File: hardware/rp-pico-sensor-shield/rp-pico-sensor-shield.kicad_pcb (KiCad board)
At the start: 2 copper layers, 87 x 65 mm, 39 parts, among them J1 Barrel_Jack, J10 Conn_01x04, J11 Conn_01x04, J12 Conn_01x04, J13 Conn_01x04, J14 Conn_01x04, J15 Conn_01x04, J16 Conn_01x04, J17 Conn_01x03, J18 Conn_01x03, J19 Conn_01x03, J2 Conn_01x04, J20 Conn_01x03, J21 Conn_01x03, J22 Conn_01x03, J23 Conn_01x04, J24 Screw Terminal, J25 Conn_01x04, J26 I2C0, J27 I2C1, J28 AGND, J29 Conn_01x03, J3 Conn_01x04, J4 Conn_01x04, J5 Conn_01x04, J6 Conn_01x04, J7 Conn_01x04, J8 Conn_01x04, J9 Conn_01x04, Q1 DMG2305UX, SW1 SW_Push, U1 NCP1117-5.0_SOT223, U2 Pico

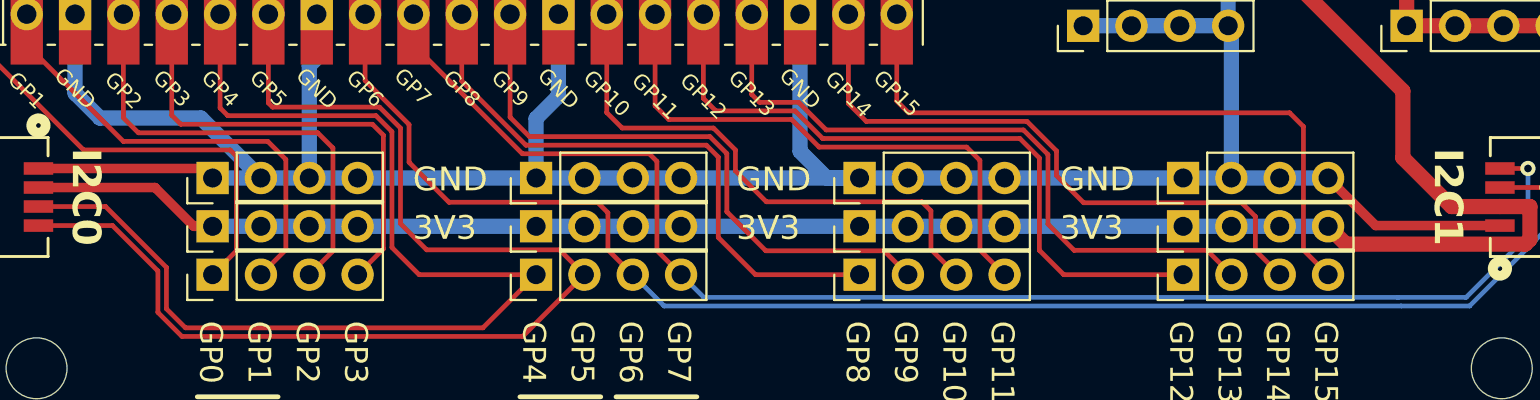
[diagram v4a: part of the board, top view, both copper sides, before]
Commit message: added qwiic logo
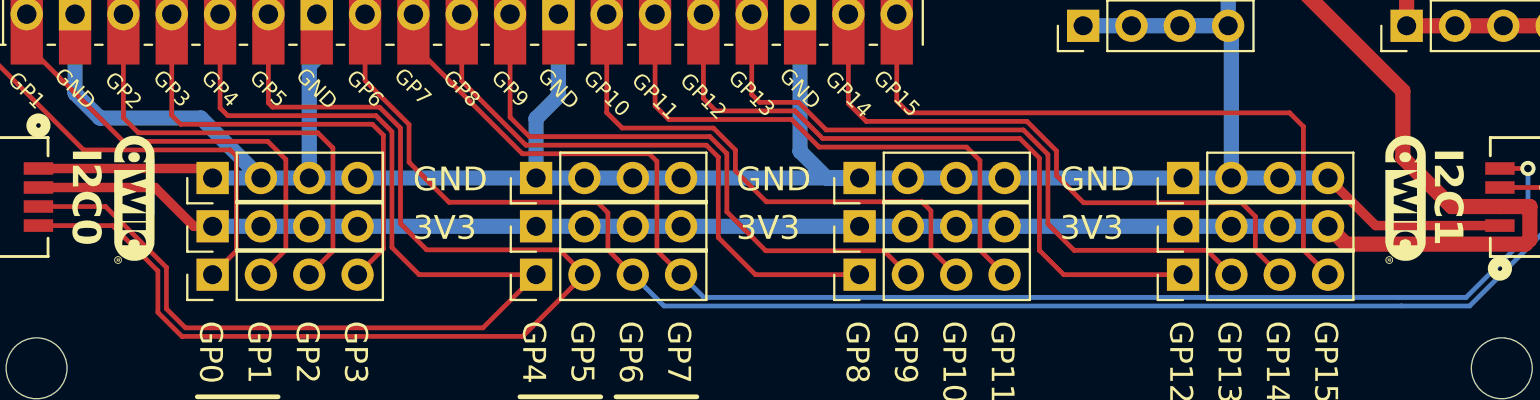
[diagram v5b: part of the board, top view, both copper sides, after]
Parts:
- added G***: LOGO, LOGO, F.Cu at (127.0, 101.1)
- added G***: LOGO, LOGO, F.Cu at (60.2, 101.1)

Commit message: updated sensor shield layout
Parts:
- added R1: 100, Resistor_SMD:R_1206_3216Metric_Pad1.30x1.75mm_HandSolder, F.Cu at (106.3, 80.8)
- added R2: 100, Resistor_SMD:R_1206_3216Metric_Pad1.30x1.75mm_HandSolder, F.Cu at (106.3, 84.1)
- moved J29 4.96 mm to (112.0, 82.6), turned to 90 degrees
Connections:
- J29 pad 1: SWDIO -> Net-(J29-Pin_1)
- J29 pad 3: SWCLK -> Net-(J29-Pin_3)
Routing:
- net GND: track 380.3 -> 394.8 mm
- net Net-(J29-Pin_3): track 0.00 -> 5.70 mm
- net Net-(J29-Pin_1): track 0.00 -> 5.65 mm
- net GPIO6: track 79.1 -> 74.2 mm, vias 1 -> 0
- net +3.3V: track 223.4 -> 219.5 mm
- net GPIO7: track 74.8 -> 71.1 mm, vias 1 -> 0
- net SWDIO: track 6.34 -> 5.17 mm
- net SWCLK: track 6.34 -> 5.17 mm

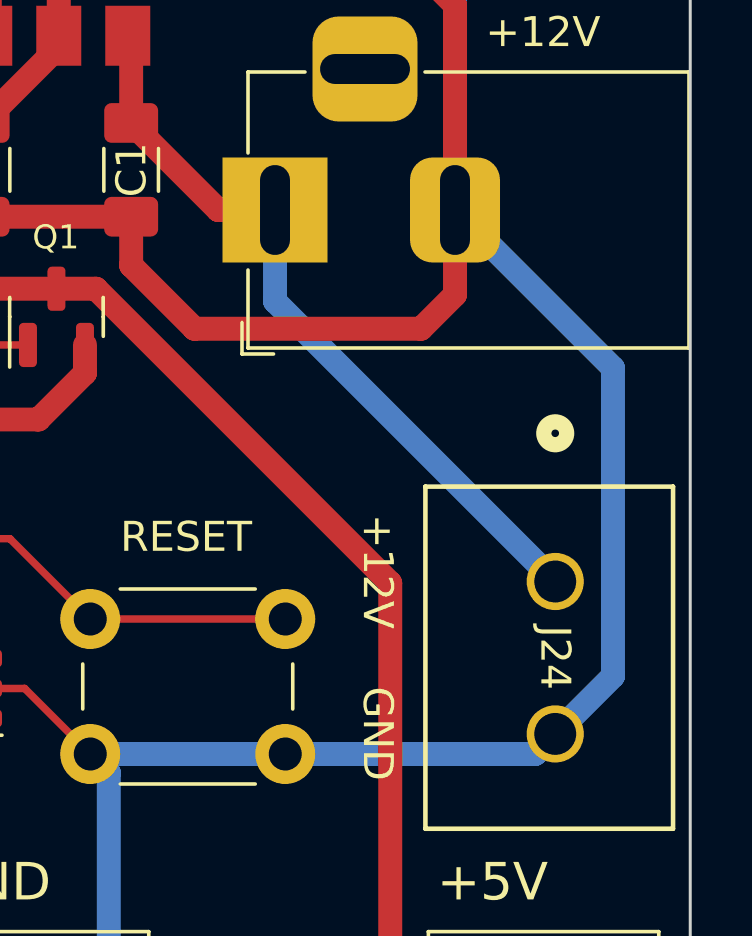
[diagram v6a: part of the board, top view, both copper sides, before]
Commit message: tweaked trace size
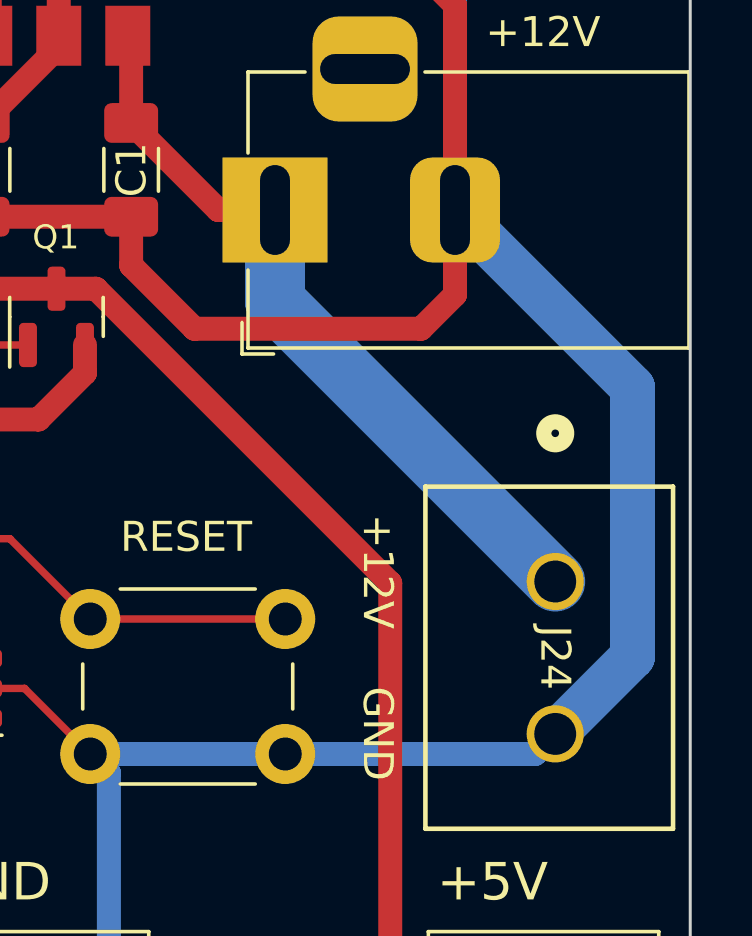
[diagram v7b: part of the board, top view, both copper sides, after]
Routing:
- net GND: track 394.8 -> 395.4 mm
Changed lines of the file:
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@@
   (segment (start 118.364 60.921) (end 118.251 60.808) (width 0.8) (layer "F.Cu") (net 1))
   (segment (start 121.265 66.6165) (end 118.364 63.7155) (width 0.8) (layer "F.Cu") (net 1))
-  (segment (start 123.159 66.6165) (end 123.159 69.659) (width 0.8) (layer "B.Cu") (net 1))
-  (segment (start 123.159 69.659) (end 132.5 79) (width 0.8) (layer "B.Cu") (net 1))
+  (segment (start 123.159 66.6165) (end 123.159 69.659) (width 2) (layer "B.Cu") (net 1))
+  (segment (start 123.159 69.659) (end 132.5 79) (width 2) (layer "B.Cu") (net 1))
   (segment (start 125.675 52.675) (end 127.4 54.4) (width 0.8) (layer "F.Cu") (net 2))
   (segment (start 118.364 66.8405) (end 113.411 66.8405) (width 0.8) (layer "F.Cu") (net 2))
@@
   (segment (start 86.33 100) (end 88.87 100) (width 0.8) (layer "B.Cu") (net 2))
   (segment (start 96.525 100) (end 95.123 98.598) (width 0.8) (layer "B.Cu") (net 2))
-  (segment (start 132.5 84.08) (end 134.425 82.155) (width 0.8) (layer "B.Cu") (net 2))
   (segment (start 96.25 65) (end 93.71 65) (width 0.8) (layer "B.Cu") (net 2))
   (segment (start 98.25 100) (end 96.525 100) (width 0.8) (layer "B.Cu") (net 2))
@@
   (segment (start 129.159 66.6165) (end 129.159 59.584) (width 0.8) (layer "B.Cu") (net 2))
   (segment (start 97.425 82.5) (end 95.123 80.198) (width 0.8) (layer "B.Cu") (net 2))
+  (segment (start 135.075 81.505) (end 135.075 72.5325) (width 1.5) (layer "B.Cu") (net 2))
   (segment (start 69.33 94.095) (end 69.723 93.702) (width 0.8) (layer "B.Cu") (net 2))
-  (segment (start 134.425 82.155) (end 134.425 71.8825) (width 0.8) (layer "B.Cu") (net 2))
   (segment (start 93.71 65) (end 84.33 65) (width 0.8) (layer "B.Cu") (net 2))
   (segment (start 66.79 100) (end 69.33 100) (width 0.8) (layer "B.Cu") (net 2))
@@
   (segment (start 129.159 59.584) (end 127.325 57.75) (width 0.8) (layer "B.Cu") (net 2))
   (segment (start 69.33 100) (end 71.87 100) (width 0.8) (layer "B.Cu") (net 2))
+  (segment (start 135.075 72.5325) (end 129.159 66.6165) (width 1.5) (layer "B.Cu") (net 2))
   (segment (start 66.79 100) (end 64.25 100) (width 0.8) (layer "B.Cu") (net 2))
   (segment (start 81.25 100) (end 83.79 100) (width 0.8) (layer "B.Cu") (net 2))
@@
   (segment (start 95.123 98.598) (end 95.123 91.39) (width 0.8) (layer "B.Cu") (net 2))
   (segment (start 99.973 82.5) (end 97.425 82.5) (width 0.8) (layer "B.Cu") (net 2))
+  (segment (start 132.5 84.08) (end 135.075 81.505) (width 1.5) (layer "B.Cu") (net 2))
   (segment (start 57.023 73.61) (end 57.023 67.038) (width 0.8) (layer "B.Cu") (net 2))
-  (segment (start 134.425 71.8825) (end 129.159 66.6165) (width 0.8) (layer "B.Cu") (net 2))
   (segment (start 98.25 100) (end 100.79 100) (width 0.8) (layer "B.Cu") (net 2))
   (segment (start 123.5 84.75) (end 131.83 84.75) (width 0.8) (layer "B.Cu") (net 2))

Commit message: kicad v8 upgrade
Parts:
- removed REF** (x4): MountingHole_3.2mm_M3, MountingHole:MountingHole_3.2mm_M3
- added H1: MountingHole, MountingHole:MountingHole_3.2mm_M3_ISO7380_Pad, F.Cu at (55.0, 55.0)
- added H2: MountingHole, MountingHole:MountingHole_3.2mm_M3_ISO7380_Pad, F.Cu at (132.0, 55.0)
- added H3: MountingHole, MountingHole:MountingHole_3.2mm_M3_ISO7380_Pad, F.Cu at (55.0, 110.0)
- added H4: MountingHole, MountingHole:MountingHole_3.2mm_M3_ISO7380_Pad, F.Cu at (132.0, 110.0)
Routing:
- net +3.3V: track 219.5 -> 218.9 mm
